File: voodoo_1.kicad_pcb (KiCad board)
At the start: 2 copper layers, 64.4 x 41 mm, 41 parts, among them Q1 2N2222, Q2 2N2222, U1 LM308

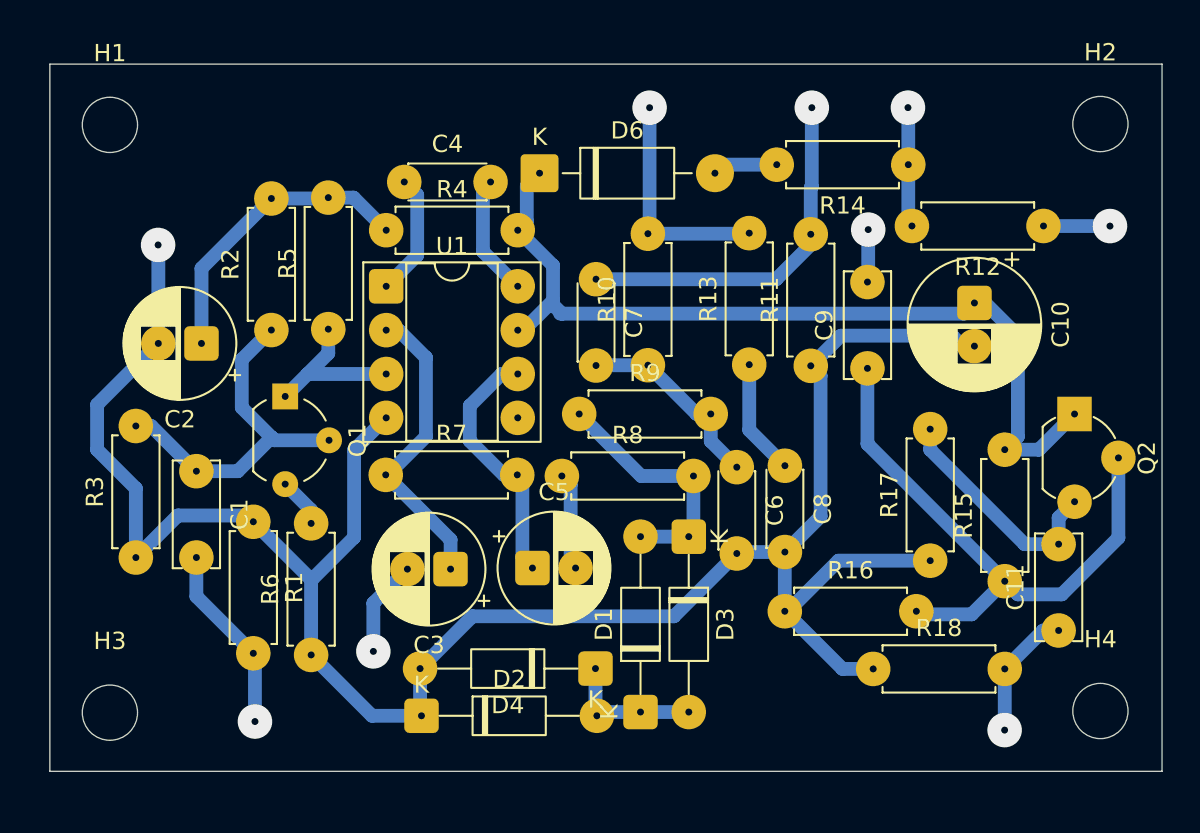
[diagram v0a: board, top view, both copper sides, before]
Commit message: 2n2222のピンアサイン修正、配置を詰めた。
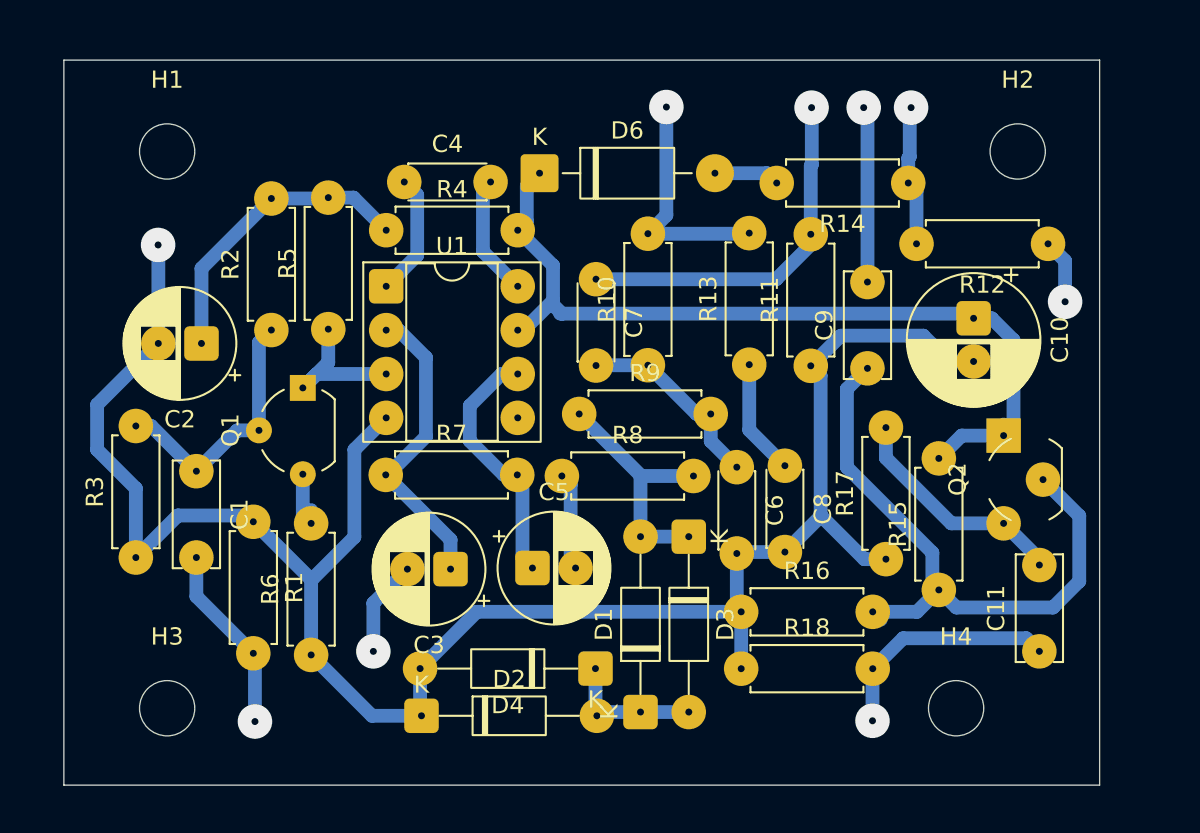
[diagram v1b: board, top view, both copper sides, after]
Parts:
- moved H4 8.36 mm to (92.7, 114.5)
- moved R18 7.65 mm to (80.2, 112.3)
- moved Q2 6.83 mm to (97.0, 103.8), turned to 90 degrees
- moved H2 5.05 mm to (96.3, 82.3)
- moved Q1 4.62 mm to (54.8, 101.0), turned to 90 degrees
- moved R15 3.85 mm to (91.7, 107.7)
- moved H1 3.66 mm to (47.0, 82.3)
- moved H3 3.32 mm to (47.0, 114.5)
- moved R17 2.57 mm to (88.6, 105.9)
- moved R16 2.53 mm to (80.2, 109.0)
- moved C11 1.65 mm to (97.5, 111.3)
- moved R12 1.07 mm to (98.0, 87.6)
- moved R14 1.06 mm to (89.9, 84.1)
- moved C10 0.89 mm to (93.7, 92.0)
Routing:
- net GND: track 126.1 -> 117.1 mm
- net Net-(C9-Pad2): track 3.06 -> 10.2 mm
- net Net-(SW1B-C): track 7.85 -> 13.7 mm
- net Net-(Q1-B): track 20.8 -> 15.3 mm
- net Net-(D6-K): track 51.9 -> 49.4 mm
- net Net-(Q2-B): track 34.4 -> 36.5 mm
- net Net-(Q1-E): track 2.90 -> 3.82 mm
- net +9V: track 7.05 -> 7.90 mm
- net Net-(D6-A): track 3.79 -> 4.51 mm
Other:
- board size 64.4 x 41 mm -> 60 x 42 mm

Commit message: C8のコンデンサ470pF -> 4700pF
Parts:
- C8: value 470p -> 4700p
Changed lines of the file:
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@@
 			)
 		)
-		(property "Value" "470p"
+		(property "Value" "4700p"
 			(at 2.5 2.2 90)
 			(layer "F.Fab")

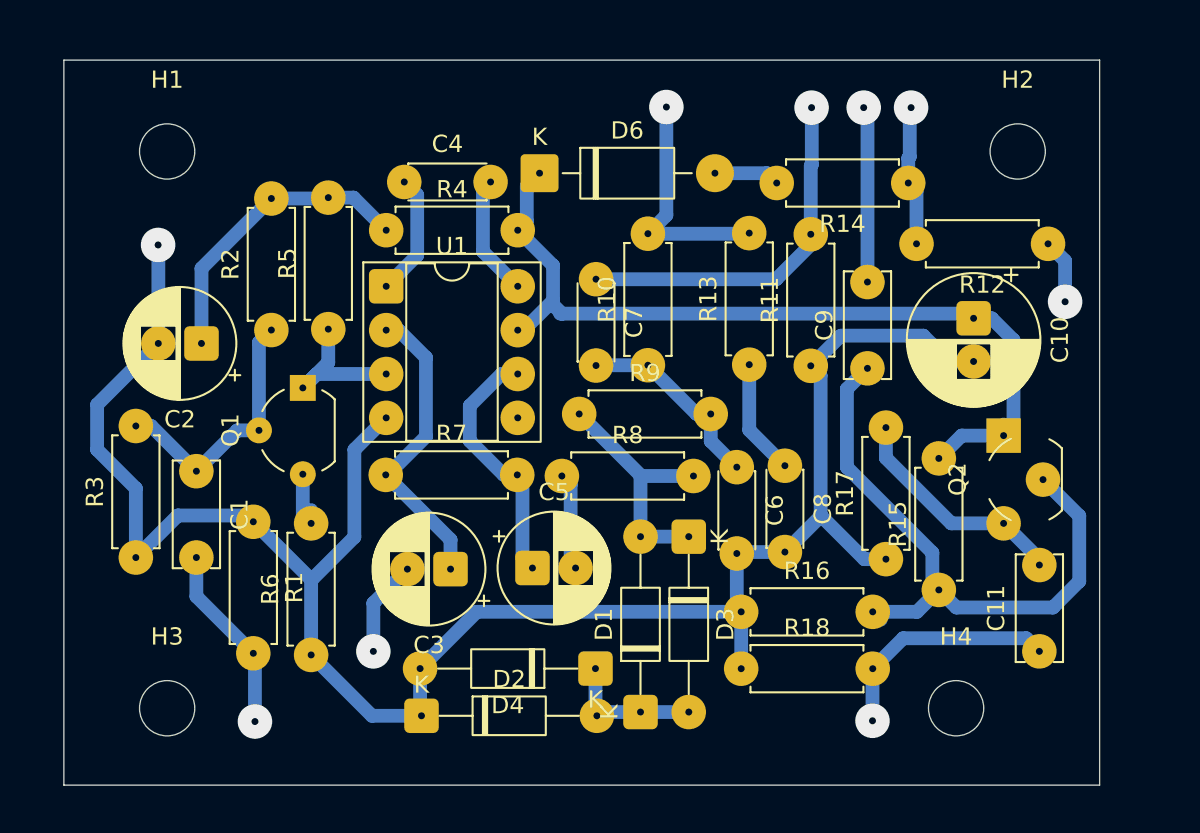
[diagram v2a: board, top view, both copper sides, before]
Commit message: 配線を修正
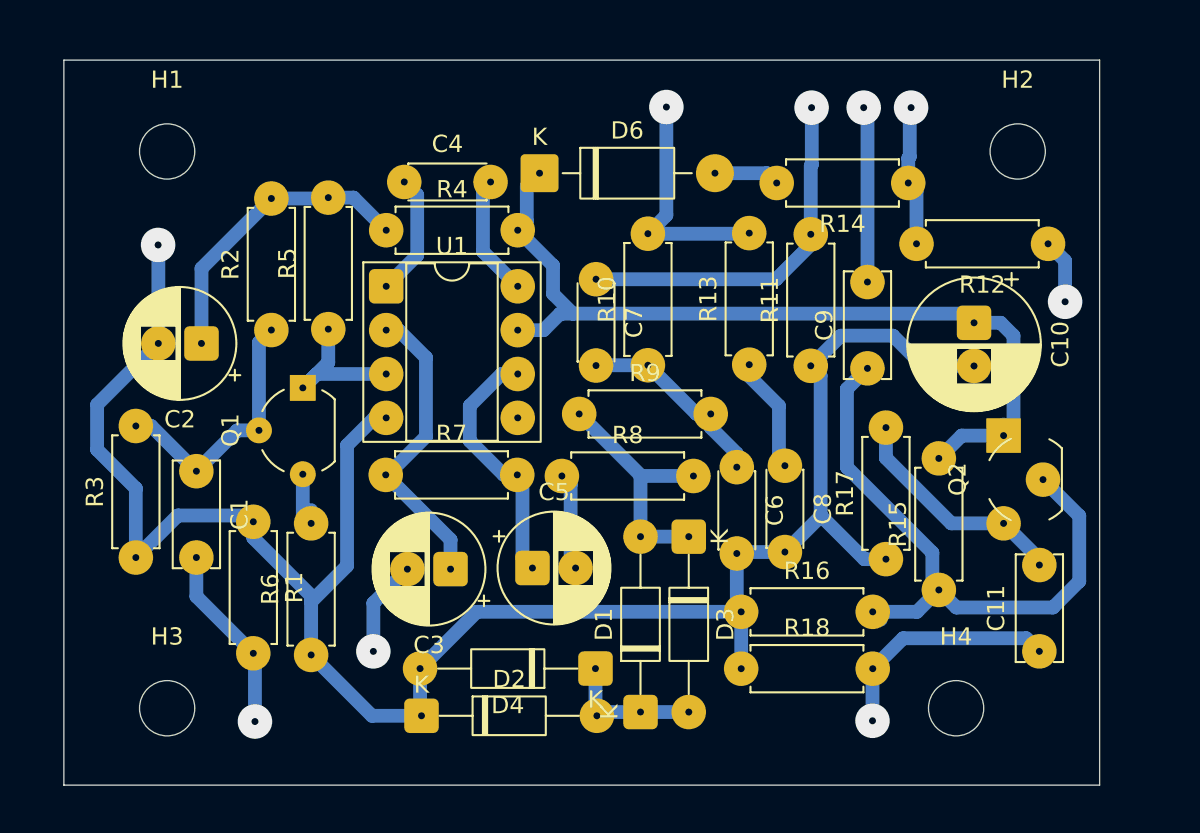
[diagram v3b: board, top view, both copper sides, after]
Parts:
- C8: value 4700p -> 470p
- moved C10 0.26 mm to (93.7, 92.2)
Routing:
- net GND: track 117.1 -> 119.3 mm
- net Net-(D6-K): track 49.4 -> 50.6 mm
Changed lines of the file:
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@@
 	(footprint "Capacitor_THT:CP_Radial_D7.5mm_P2.50mm"
 		(layer "F.Cu")
-		(at 93.698877 91.958361 -90)
+		(at 93.72448 92.217575 -90)
 		(descr "CP, Radial series, Radial, pin pitch=2.50mm, diameter=7.5mm, height=8mm, Electrolytic Capacitor")
 		(tags "CP Radial series Radial pin pitch 2.50mm diameter 7.5mm height 8mm Electrolytic Capacitor")
@@
 			)
 		)
-		(property "Value" "4700p"
+		(property "Value" "470p"
 			(at 2.5 2.2 90)
 			(layer "F.Fab")
@@
 	)
 	(segment
-		(start 59.672357 97.723607)
-		(end 57.82923 99.566734)
-		(width 0.8)
-		(layer "B.Cu")
-		(net 4)
-	)
-	(segment
 		(start 46.47112 93.412688)
 		(end 46.47112 87.720243)
@@
 	)
 	(segment
+		(start 57.404 99.314)
+		(end 58.994393 97.723607)
+		(width 0.8)
+		(layer "B.Cu")
+		(net 4)
+	)
+	(segment
 		(start 84.836 103.429739)
 		(end 82.768715 105.497024)
@@
 	)
 	(segment
+		(start 90.780575 94.717575)
+		(end 93.72448 94.717575)
+		(width 0.8)
+		(layer "B.Cu")
+		(net 4)
+	)
+	(segment
 		(start 80.235789 112.254812)
 		(end 80.235789 108.960867)
@@
 	)
 	(segment
-		(start 90.790303 92.964)
-		(end 92.284664 94.458361)
+		(start 83.180174 105.908483)
+		(end 82.768715 105.497024)
 		(width 0.8)
 		(layer "B.Cu")
@@
 	)
 	(segment
-		(start 86.012652 92.964)
-		(end 90.790303 92.964)
+		(start 64.922175 108.960867)
+		(end 61.634701 112.248341)
 		(width 0.8)
 		(layer "B.Cu")
@@
 	)
 	(segment
-		(start 55.366363 107.093098)
-		(end 55.323153 107.093098)
+		(start 84.266696 94.709956)
+		(end 84.836 95.27926)
 		(width 0.8)
 		(layer "B.Cu")
@@
 	)
 	(segment
-		(start 83.180174 105.908483)
-		(end 82.768715 105.497024)
+		(start 86.012652 92.964)
+		(end 89.027 92.964)
 		(width 0.8)
 		(layer "B.Cu")
@@
 	)
 	(segment
-		(start 64.922175 108.960867)
-		(end 61.634701 112.248341)
+		(start 89.027 92.964)
+		(end 90.780575 94.717575)
 		(width 0.8)
 		(layer "B.Cu")
@@
 	)
 	(segment
-		(start 84.266696 94.709956)
-		(end 84.836 95.27926)
+		(start 55.323153 108.379847)
+		(end 57.404 106.299)
 		(width 0.8)
 		(layer "B.Cu")
@@
 	)
 	(segment
-		(start 86.012652 92.964)
-		(end 84.266696 94.709956)
+		(start 55.323153 108.028153)
+		(end 55.323153 108.379847)
 		(width 0.8)
 		(layer "B.Cu")
@@
 	)
 	(segment
-		(start 92.284664 94.458361)
-		(end 93.698877 94.458361)
+		(start 84.266696 94.709956)
+		(end 86.012652 92.964)
 		(width 0.8)
 		(layer "B.Cu")
@@
 	)
 	(segment
-		(start 57.82923 104.630231)
-		(end 55.366363 107.093098)
+		(start 51.973703 103.743648)
+		(end 51.973703 104.678703)
 		(width 0.8)
 		(layer "B.Cu")
@@
 	)
 	(segment
-		(start 57.82923 99.566734)
-		(end 57.82923 104.630231)
+		(start 61.634701 112.248341)
+		(end 61.634701 114.900734)
 		(width 0.8)
 		(layer "B.Cu")
@@
 	)
 	(segment
-		(start 61.634701 112.248341)
-		(end 61.634701 114.900734)
+		(start 55.323153 111.457851)
+		(end 55.323153 108.379847)
 		(width 0.8)
 		(layer "B.Cu")
@@
 	)
 	(segment
+		(start 51.973703 104.147675)
+		(end 51.973703 103.743648)
+		(width 0.8)
+		(layer "B.Cu")
+		(net 4)
+	)
+	(segment
+		(start 57.404 106.299)
+		(end 57.404 99.314)
+		(width 0.8)
+		(layer "B.Cu")
+		(net 4)
+	)
+	(segment
 		(start 80.066238 105.497024)
 		(end 79.981364 105.581898)
@@
 	)
 	(segment
-		(start 45.170131 101.812131)
-		(end 42.926 99.568)
+		(start 51.973703 104.678703)
+		(end 55.323153 108.028153)
 		(width 0.8)
 		(layer "B.Cu")
@@
 	)
 	(segment
-		(start 55.323153 107.093098)
-		(end 51.973703 103.743648)
+		(start 45.170131 101.812131)
+		(end 42.926 99.568)
 		(width 0.8)
 		(layer "B.Cu")
@@
 	)
 	(segment
-		(start 55.323153 111.457851)
-		(end 55.323153 107.093098)
+		(start 58.994393 97.723607)
+		(end 59.672357 97.723607)
 		(width 0.8)
 		(layer "B.Cu")
@@
 	)
 	(segment
+		(start 78.472077 98.284077)
+		(end 79.981364 99.793364)
+		(width 0.8)
+		(layer "B.Cu")
+		(net 11)
+	)
+	(segment
 		(start 71.845013 94.676291)
 		(end 71.827201 94.694103)
@@
 	)
 	(segment
-		(start 78.472077 97.499419)
-		(end 78.472077 99.072611)
+		(start 79.981364 99.793364)
+		(end 79.981364 100.581898)
 		(width 0.8)
 		(layer "B.Cu")
@@
 	)
 	(segment
-		(start 78.472077 99.072611)
-		(end 79.981364 100.581898)
+		(start 78.472077 97.499419)
+		(end 78.472077 98.284077)
 		(width 0.8)
 		(layer "B.Cu")
@@
 	)
 	(segment
-		(start 80.702571 98.43088)
-		(end 82.768715 100.497024)
+		(start 80.702571 95.307571)
+		(end 80.702571 94.642627)
+		(width 0.8)
+		(layer "B.Cu")
+		(net 13)
+	)
+	(segment
+		(start 82.423 97.028)
+		(end 80.702571 95.307571)
 		(width 0.8)
 		(layer "B.Cu")
@@
 	)
 	(segment
-		(start 80.702571 94.642627)
-		(end 80.702571 98.43088)
+		(start 82.423 100.151309)
+		(end 82.423 97.028)
+		(width 0.8)
+		(layer "B.Cu")
+		(net 13)
+	)
+	(segment
+		(start 82.768715 100.497024)
+		(end 82.423 100.151309)
 		(width 0.8)
 		(layer "B.Cu")
@@
 	)
 	(segment
-		(start 67.818 84.287527)
-		(end 67.818 86.329598)
+		(start 93.19511 91.688205)
+		(end 93.72448 92.217575)
 		(width 0.8)
 		(layer "B.Cu")
@@
 	)
 	(segment
-		(start 69.337116 90.936884)
-		(end 69.337116 91.175321)
+		(start 95.265575 92.217575)
+		(end 96.012 92.964)
 		(width 0.8)
 		(layer "B.Cu")
@@
 	)
 	(segment
-		(start 68.554879 83.550648)
-		(end 67.818 84.287527)
+		(start 69.337116 90.540321)
+		(end 70.485 91.688205)
 		(width 0.8)
 		(layer "B.Cu")
@@
 	)
 	(segment
-		(start 95.437348 98.751489)
-		(end 93.007125 98.751489)
+		(start 67.818 84.287527)
+		(end 67.818 86.329598)
 		(width 0.8)
 		(layer "B.Cu")
@@
 	)
 	(segment
-		(start 67.630393 92.643607)
-		(end 67.292357 92.643607)
+		(start 93.72448 92.217575)
+		(end 95.265575 92.217575)
 		(width 0.8)
 		(layer "B.Cu")
@@
 	)
 	(segment
-		(start 69.85 91.688205)
-		(end 93.126894 91.688205)
+		(start 68.554879 83.550648)
+		(end 67.818 84.287527)
+		(width 0.8)
+		(layer "B.Cu")
+		(net 27)
+	)
+	(segment
+		(start 95.437348 98.751489)
+		(end 93.007125 98.751489)
 		(width 0.8)
 		(layer "B.Cu")
@@
 	)
 	(segment
-		(start 93.698877 91.958361)
-		(end 94.752361 91.958361)
+		(start 67.292357 86.855241)
+		(end 69.337116 88.9)
 		(width 0.8)
 		(layer "B.Cu")
@@
 	)
 	(segment
-		(start 69.337116 91.175321)
-		(end 69.85 91.688205)
+		(start 96.012 98.176837)
+		(end 95.437348 98.751489)
 		(width 0.8)
 		(layer "B.Cu")
@@
 	)
 	(segment
-		(start 67.292357 86.855241)
-		(end 69.337116 88.9)
+		(start 70.485 91.688205)
+		(end 93.19511 91.688205)
 		(width 0.8)
 		(layer "B.Cu")
@@
 	)
 	(segment
-		(start 69.337116 90.936884)
-		(end 67.630393 92.643607)
+		(start 69.337116 88.9)
+		(end 69.337116 90.540321)
 		(width 0.8)
 		(layer "B.Cu")
@@
 	)
 	(segment
-		(start 94.752361 91.958361)
-		(end 96.012 93.218)
+		(start 68.790181 92.643607)
+		(end 69.745583 91.688205)
 		(width 0.8)
 		(layer "B.Cu")
@@
 	)
 	(segment
-		(start 96.012 98.176837)
-		(end 95.437348 98.751489)
+		(start 69.85 91.688205)
+		(end 70.485 91.688205)
 		(width 0.8)
 		(layer "B.Cu")
@@
 	)
 	(segment
-		(start 69.337116 88.9)
-		(end 69.337116 90.936884)
+		(start 67.292357 92.643607)
+		(end 68.790181 92.643607)
 		(width 0.8)
 		(layer "B.Cu")
@@
 	)
 	(segment
-		(start 96.012 93.218)
+		(start 96.012 92.964)
 		(end 96.012 98.176837)
 		(width 0.8)

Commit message: 配線を修正
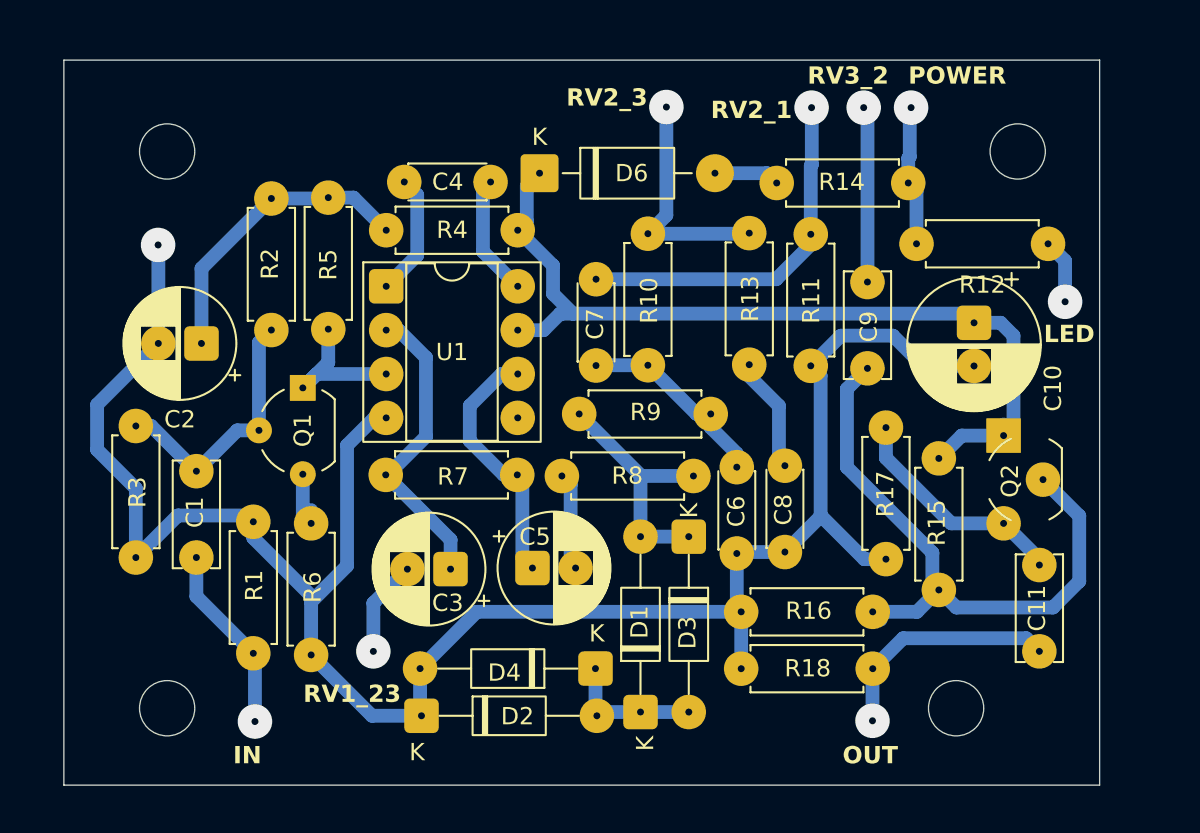
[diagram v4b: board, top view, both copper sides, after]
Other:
- board text added: "IN"
- board text added: "LED"
- board text added: "OUT"
- board text added: "POWER"
- board text added: "RV1_23"
- board text added: "RV2_1"
- board text added: "RV2_3"
- board text added: "RV3_2"

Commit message: ベタ追加
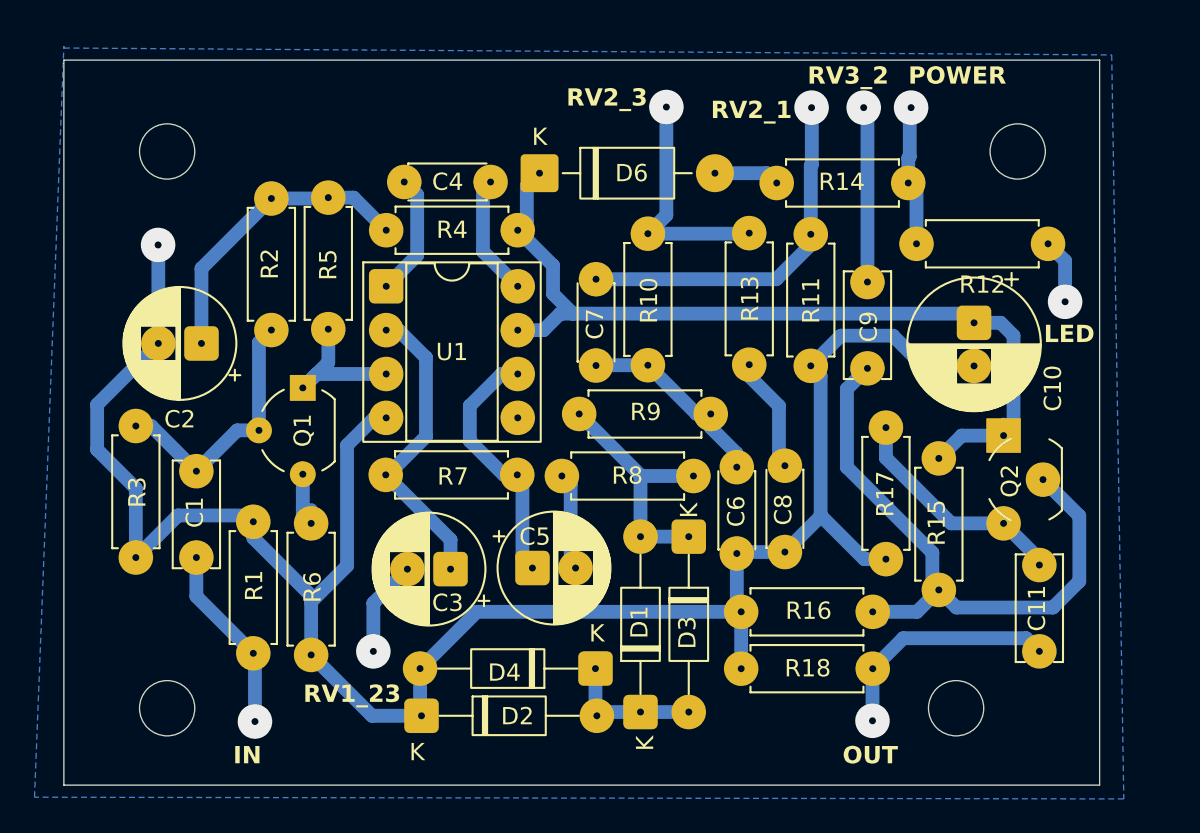
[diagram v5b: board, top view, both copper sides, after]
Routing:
- added copper zone on B.Cu, net (none)
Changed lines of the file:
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@@
 		(net 27)
+	)
+	(zone
+		(net 0)
+		(net_name "")
+		(layer "B.Cu")
+		(hatch edge 0.5)
+		(connect_pads
+			(clearance 1)
+		)
+		(min_thickness 0.25)
+		(filled_areas_thickness no)
+		(fill yes
+			(thermal_gap 0.5)
+			(thermal_bridge_width 0.5)
+			(island_removal_mode 1)
+			(island_area_min 10)
+		)
+		(polygon
+			(pts
+				(xy 41 76.3) (xy 101.7 76.7) (xy 102.4 119.8) (xy 39.3 119.7) (xy 41 76.2)
+			)
+		)
 	)
 	(embedded_fonts no)
